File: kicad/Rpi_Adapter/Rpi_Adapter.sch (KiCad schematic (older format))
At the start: 12 parts, among them P1 Raspberry PI, SW1 SW_Push, U1 SGM811

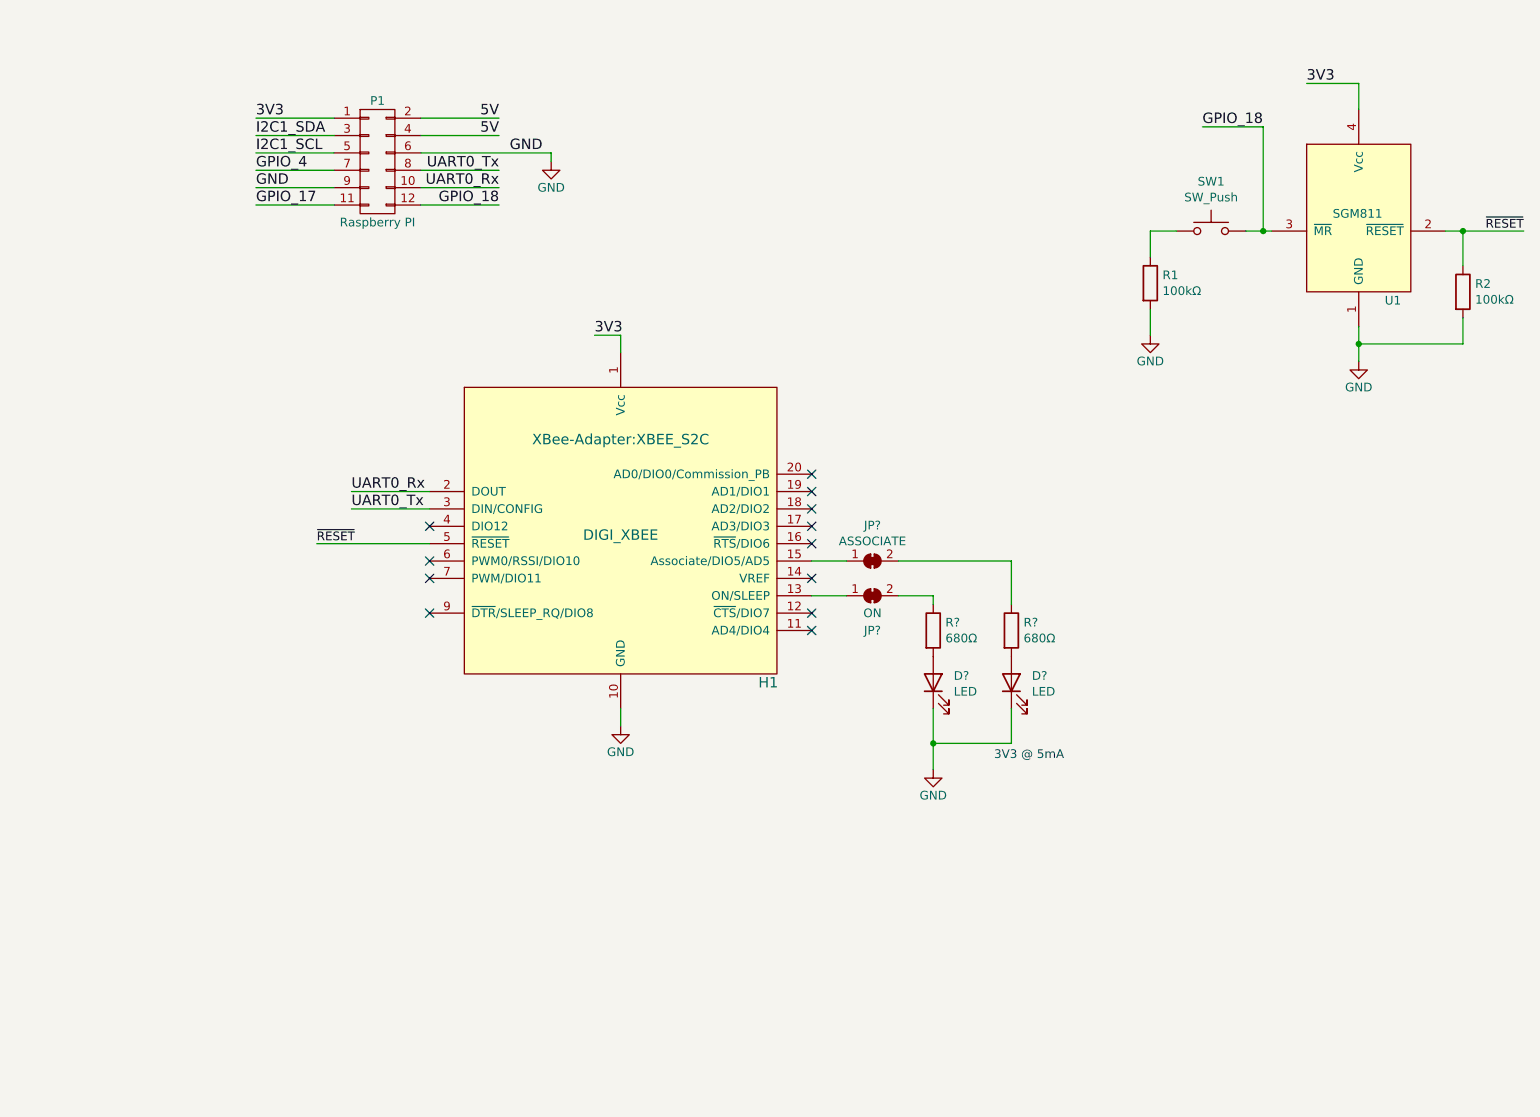
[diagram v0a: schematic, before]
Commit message: Updated the 3d view and a new layout
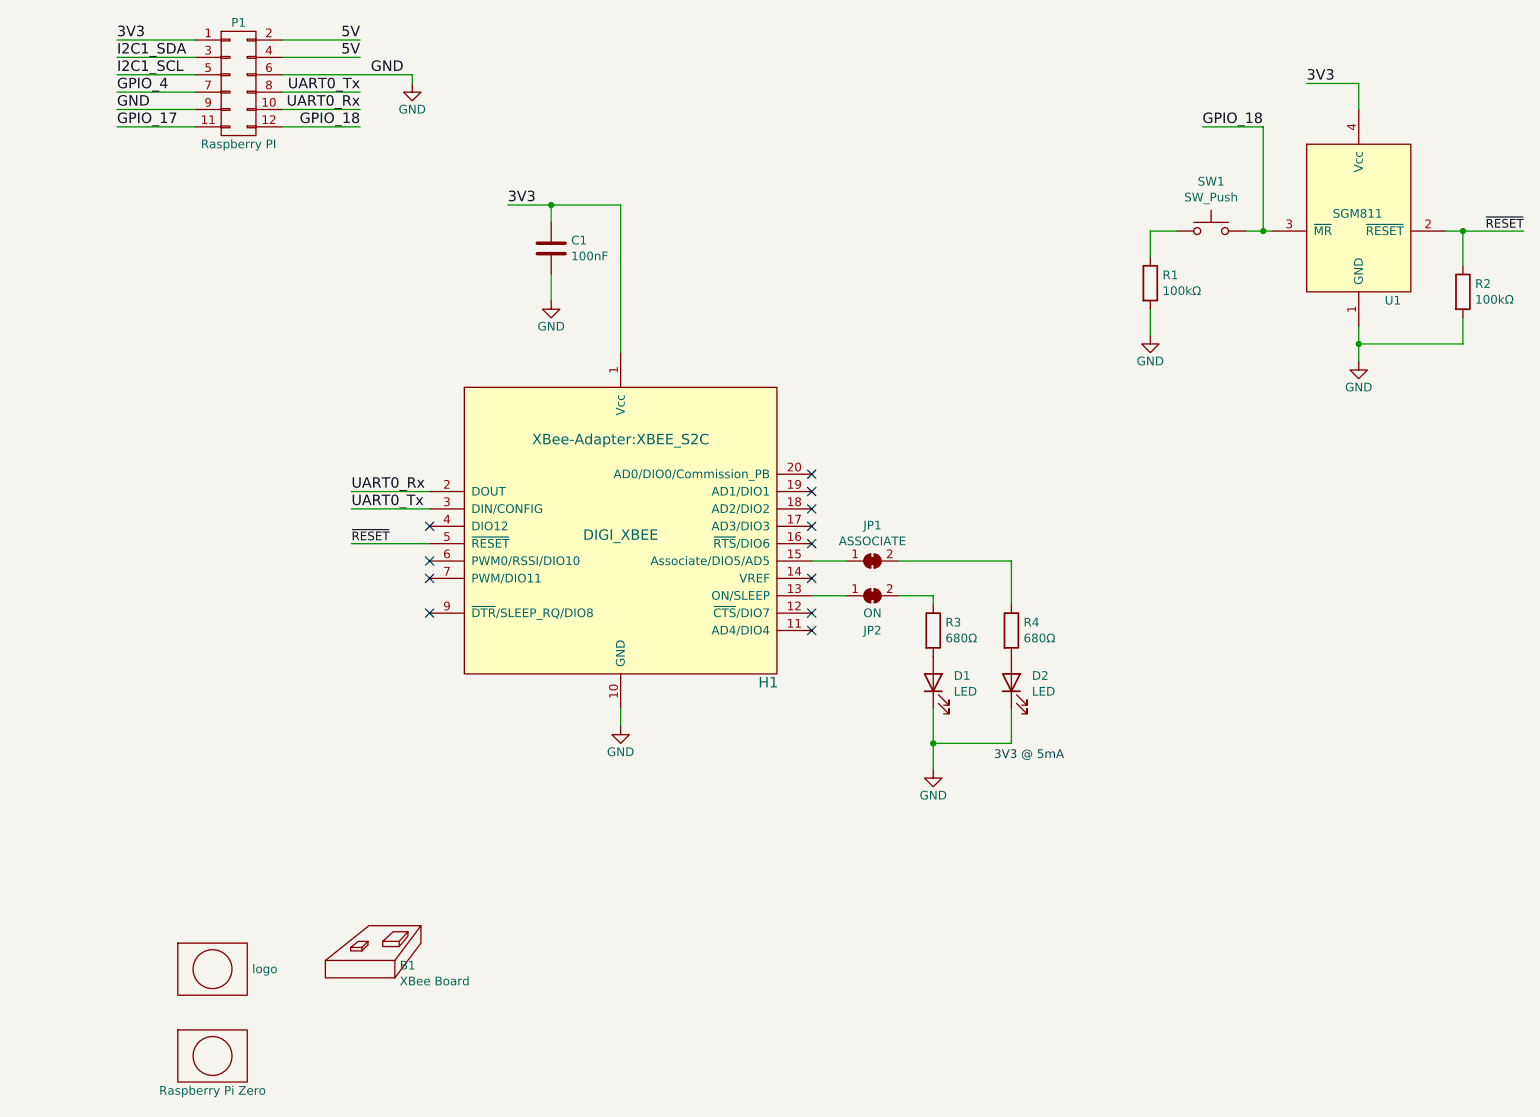
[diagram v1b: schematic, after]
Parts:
- added B1: XBee Board, mech:Board Ref, symbol mech:board
- added B2: Raspberry Pi Zero, mech:Board Ref, symbol mech:logo
- added C1: 100nF, Capacitor_SMD:C_0805_2012Metric, symbol Device:C
- added L1: logo, XBee-Adapter:MyBasic_rounded_50_1, symbol mech:logo
- D1, D2: renamed from D?; footprint (none) -> LED_SMD:LED_0805_2012Metric
- JP1, JP2: renamed from JP?; footprint (none) -> Jumper:SolderJumper-2_P1.3mm_Bridged_RoundedPad1.0x1.5mm
- R3, R4: renamed from R?; footprint (none) -> Resistor_SMD:R_0805_2012Metric
- SW1: footprint GoldCap-Check:SPST_FSM2JSMAA -> Connector_PinHeader_2.54mm:PinHeader_1x02_P2.54mm_Vertical
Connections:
- net 3V3: now also C1.1
- net GND: now also C1.2
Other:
- moved on the sheet: P1
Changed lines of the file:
@@
 Comment4 ""
 $EndDescr
-Text Label 4500 2900 0    60   ~ 0
+Text Label 4000 2150 0    60   ~ 0
 3V3
 Wire Wire Line
-	4500 2900 4650 2900
-Wire Wire Line
-	4650 2900 4650 3000
+	4000 2150 4250 2150
+Wire Wire Line
+	4650 2150 4650 3000
 $Comp
 L power:GND #PWR01
@@
 L Rpi_Adapter-rescue:CONN_02X06 P1
 U 1 1 59933EB5
-P 3250 1900
-F 0 "P1" H 3250 2250 50  0000 C CNN
-F 1 "Raspberry PI" H 3250 1550 50  0000 C CNN
-F 2 "Socket_Strips:Socket_Strip_Straight_2x06_Pitch2.54mm" H 3250 700 60  0001 C CNN
-F 3 "" H 3250 700 60  0000 C CNN
-	1    3250 1900
-	1    0    0    -1
-$EndComp
-Wire Wire Line
-	3000 1650 2550 1650
-Wire Wire Line
-	3500 1850 4250 1850
-Wire Wire Line
-	3500 1950 3950 1950
-Wire Wire Line
-	3500 2050 3950 2050
-Text Label 2550 1650 0    60   ~ 0
+P 2450 1450
+F 0 "P1" H 2450 1800 50  0000 C CNN
+F 1 "Raspberry PI" H 2450 1100 50  0000 C CNN
+F 2 "Socket_Strips:Socket_Strip_Straight_2x06_Pitch2.54mm" H 2450 250 60  0001 C CNN
+F 3 "" H 2450 250 60  0000 C CNN
+	1    2450 1450
+	1    0    0    -1
+$EndComp
+Wire Wire Line
+	2200 1200 1750 1200
+Wire Wire Line
+	2700 1400 3450 1400
+Wire Wire Line
+	2700 1500 3150 1500
+Wire Wire Line
+	2700 1600 3150 1600
+Text Label 1750 1200 0    60   ~ 0
 3V3
 $Comp
 L power:GND #PWR02
 U 1 1 5993431C
-P 4250 1900
-F 0 "#PWR02" H 4250 1650 50  0001 C CNN
-F 1 "GND" H 4250 1750 50  0000 C CNN
-F 2 "" H 4250 1900 60  0000 C CNN
-F 3 "" H 4250 1900 60  0000 C CNN
-	1    4250 1900
-	1    0    0    -1
-$EndComp
-Wire Wire Line
-	4250 1850 4250 1900
-Text Label 3950 1950 2    60   ~ 0
+P 3450 1450
+F 0 "#PWR02" H 3450 1200 50  0001 C CNN
+F 1 "GND" H 3450 1300 50  0000 C CNN
+F 2 "" H 3450 1450 60  0000 C CNN
+F 3 "" H 3450 1450 60  0000 C CNN
+	1    3450 1450
+	1    0    0    -1
+$EndComp
+Wire Wire Line
+	3450 1400 3450 1450
+Text Label 3150 1500 2    60   ~ 0
 UART0_Tx
-Text Label 3950 2050 2    60   ~ 0
+Text Label 3150 1600 2    60   ~ 0
 UART0_Rx
 Wire Wire Line
-	3500 1650 3950 1650
-Wire Wire Line
-	3500 1750 3950 1750
-Wire Wire Line
-	3000 1750 2550 1750
-Wire Wire Line
-	3000 1850 2550 1850
-Wire Wire Line
-	3000 1950 2550 1950
-Wire Wire Line
-	3000 2050 2550 2050
-Wire Wire Line
-	3000 2150 2550 2150
-Wire Wire Line
-	3500 2150 3950 2150
-Text Label 2550 1750 0    60   ~ 0
+	2700 1200 3150 1200
+Wire Wire Line
+	2700 1300 3150 1300
+Wire Wire Line
+	2200 1300 1750 1300
+Wire Wire Line
+	2200 1400 1750 1400
+Wire Wire Line
+	2200 1500 1750 1500
+Wire Wire Line
+	2200 1600 1750 1600
+Wire Wire Line
+	2200 1700 1750 1700
+Wire Wire Line
+	2700 1700 3150 1700
+Text Label 1750 1300 0    60   ~ 0
 I2C1_SDA
-Text Label 2550 1850 0    60   ~ 0
+Text Label 1750 1400 0    60   ~ 0
 I2C1_SCL
-Text Label 2550 1950 0    60   ~ 0
+Text Label 1750 1500 0    60   ~ 0
 GPIO_4
-Text Label 2550 2050 0    60   ~ 0
+Text Label 1750 1600 0    60   ~ 0
 GND
-Text Label 2550 2150 0    60   ~ 0
+Text Label 1750 1700 0    60   ~ 0
 GPIO_17
-Text Label 3950 1650 2    60   ~ 0
+Text Label 3150 1200 2    60   ~ 0
 5V
-Text Label 3950 1750 2    60   ~ 0
+Text Label 3150 1300 2    60   ~ 0
 5V
-Text Label 4200 1850 2    60   ~ 0
+Text Label 3400 1400 2    60   ~ 0
 GND
-Text Label 3950 2150 2    60   ~ 0
+Text Label 3150 1700 2    60   ~ 0
 GPIO_18
 $Comp
@@
 F 0 "SW1" H 8050 2585 50  0000 C CNN
 F 1 "SW_Push" H 8050 2494 50  0000 C CNN
-F 2 "GoldCap-Check:SPST_FSM2JSMAA" H 8050 2500 50  0001 C CNN
+F 2 "Connector_PinHeader_2.54mm:PinHeader_1x02_P2.54mm_Vertical" H 8050 2500 50  0001 C CNN
 F 3 "~" H 8050 2500 50  0001 C CNN
 	1    8050 2300
@@
 $EndComp
 Wire Wire Line
-	3550 4100 2900 4100
+	3550 4100 3100 4100
 Text Label 8000 1700 0    60   ~ 0
 GPIO_18
@@
 Wire Wire Line
 	8350 2300 8250 2300
-Text Label 2900 4100 0    50   ~ 0
+Text Label 3100 4100 0    50   ~ 0
 ~RESET
 Wire Wire Line
@@
 	5750 4400 5950 4400
 $Comp
-L Jumper:SolderJumper_2_Bridged JP?
+L Jumper:SolderJumper_2_Bridged JP1
 U 1 1 612FC7BD
 P 6100 4200
-F 0 "JP?" H 6100 4405 50  0000 C CNN
+F 0 "JP1" H 6100 4405 50  0000 C CNN
 F 1 "ASSOCIATE" H 6100 4314 50  0000 C CNN
-F 2 "" H 6100 4200 50  0001 C CNN
+F 2 "Jumper:SolderJumper-2_P1.3mm_Bridged_RoundedPad1.0x1.5mm" H 6100 4200 50  0001 C CNN
 F 3 "~" H 6100 4200 50  0001 C CNN
 	1    6100 4200
@@
 $EndComp
 $Comp
-L Jumper:SolderJumper_2_Bridged JP?
+L Jumper:SolderJumper_2_Bridged JP2
 U 1 1 612FD33D
 P 6100 4400
-F 0 "JP?" H 6100 4200 50  0000 C CNN
+F 0 "JP2" H 6100 4200 50  0000 C CNN
 F 1 "ON" H 6100 4300 50  0000 C CNN
-F 2 "" H 6100 4400 50  0001 C CNN
+F 2 "Jumper:SolderJumper-2_P1.3mm_Bridged_RoundedPad1.0x1.5mm" H 6100 4400 50  0001 C CNN
 F 3 "~" H 6100 4400 50  0001 C CNN
 	1    6100 4400
@@
 $EndComp
 $Comp
-L Device:LED D?
+L Device:LED D1
 U 1 1 612FE401
 P 6450 4900
-F 0 "D?" V 6489 4782 50  0000 R CNN
+F 0 "D1" V 6489 4782 50  0000 R CNN
 F 1 "LED" V 6398 4782 50  0000 R CNN
-F 2 "" H 6450 4900 50  0001 C CNN
+F 2 "LED_SMD:LED_0805_2012Metric" H 6450 4900 50  0001 C CNN
 F 3 "~" H 6450 4900 50  0001 C CNN
 	1    6450 4900
@@
 $EndComp
 $Comp
-L Device:LED D?
+L Device:LED D2
 U 1 1 612FF5D4
 P 6900 4900
-F 0 "D?" V 6939 4782 50  0000 R CNN
+F 0 "D2" V 6939 4782 50  0000 R CNN
 F 1 "LED" V 6848 4782 50  0000 R CNN
-F 2 "" H 6900 4900 50  0001 C CNN
+F 2 "LED_SMD:LED_0805_2012Metric" H 6900 4900 50  0001 C CNN
 F 3 "~" H 6900 4900 50  0001 C CNN
 	1    6900 4900
@@
 	6450 5250 6450 5400
 $Comp
-L power:GND #PWR?
+L power:GND #PWR0101
 U 1 1 61300F5E
 P 6450 5400
-F 0 "#PWR?" H 6450 5150 50  0001 C CNN
+F 0 "#PWR0101" H 6450 5150 50  0001 C CNN
 F 1 "GND" H 6450 5250 50  0000 C CNN
 F 2 "" H 6450 5400 60  0000 C CNN
@@
 $EndComp
 $Comp
-L Device:R R?
+L Device:R R3
 U 1 1 61301AD8
 P 6450 4600
-F 0 "R?" H 6520 4646 50  0000 L CNN
+F 0 "R3" H 6520 4646 50  0000 L CNN
 F 1 "680Ω" H 6520 4555 50  0000 L CNN
-F 2 "" V 6380 4600 50  0001 C CNN
+F 2 "Resistor_SMD:R_0805_2012Metric" V 6380 4600 50  0001 C CNN
 F 3 "~" H 6450 4600 50  0001 C CNN
 	1    6450 4600
@@
 $EndComp
 $Comp
-L Device:R R?
+L Device:R R4
 U 1 1 61301FA2
 P 6900 4600
-F 0 "R?" H 6970 4646 50  0000 L CNN
+F 0 "R4" H 6970 4646 50  0000 L CNN
 F 1 "680Ω" H 6970 4555 50  0000 L CNN
-F 2 "" V 6830 4600 50  0001 C CNN
+F 2 "Resistor_SMD:R_0805_2012Metric" V 6830 4600 50  0001 C CNN
 F 3 "~" H 6900 4600 50  0001 C CNN
 	1    6900 4600
@@
 Text Notes 6800 5350 0    50   ~ 0
 3V3 @ 5mA
+$Comp
+L Device:C C1
+U 1 1 612E681C
+P 4250 2400
+F 0 "C1" H 4365 2446 50  0000 L CNN
+F 1 "100nF" H 4365 2355 50  0000 L CNN
+F 2 "Capacitor_SMD:C_0805_2012Metric" H 4288 2250 50  0001 C CNN
+F 3 "~" H 4250 2400 50  0001 C CNN
+	1    4250 2400
+	1    0    0    -1
+$EndComp
+Wire Wire Line
+	4250 2150 4250 2250
+Wire Wire Line
+	4250 2550 4250 2700
+Connection ~ 4250 2150
+Wire Wire Line
+	4250 2150 4650 2150
+$Comp
+L power:GND #PWR05
+U 1 1 612E794A
+P 4250 2700
+F 0 "#PWR05" H 4250 2450 50  0001 C CNN
+F 1 "GND" H 4250 2550 50  0000 C CNN
+F 2 "" H 4250 2700 60  0000 C CNN
+F 3 "" H 4250 2700 60  0000 C CNN
+	1    4250 2700
+	1    0    0    -1
+$EndComp
+$Comp
+L mech:logo L1
+U 1 1 612E7975
+P 2300 6550
+F 0 "L1" H 2300 6550 50  0001 C CNN
+F 1 "logo" H 2528 6550 50  0000 L CNN
+F 2 "XBee-Adapter:MyBasic_rounded_50_1" H 2300 6550 50  0001 C CNN
+F 3 "" H 2300 6550 50  0001 C CNN
+	1    2300 6550
+	1    0    0    -1
+$EndComp
+$Comp
+L mech:board B1
+U 1 1 612EB311
+P 3150 6550
+F 0 "B1" H 3378 6571 50  0000 L CNN
+F 1 "XBee Board" H 3378 6480 50  0000 L CNN
+F 2 "mech:Board Ref" H 3150 6550 50  0001 C CNN
+F 3 "" H 3150 6550 50  0001 C CNN
+	1    3150 6550
+	1    0    0    -1
+$EndComp
+$Comp
+L mech:logo B2
+U 1 1 612ECCDF
+P 2300 7050
+F 0 "B2" H 2300 7050 50  0001 C CNN
+F 1 "Raspberry Pi Zero" H 2300 6850 50  0000 C CNN
+F 2 "mech:Board Ref" H 2300 7050 50  0001 C CNN
+F 3 "" H 2300 7050 50  0001 C CNN
+	1    2300 7050
+	1    0    0    -1
+$EndComp
 $EndSCHEMATC

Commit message: Completed the layout and routing, Sent to OSH Park
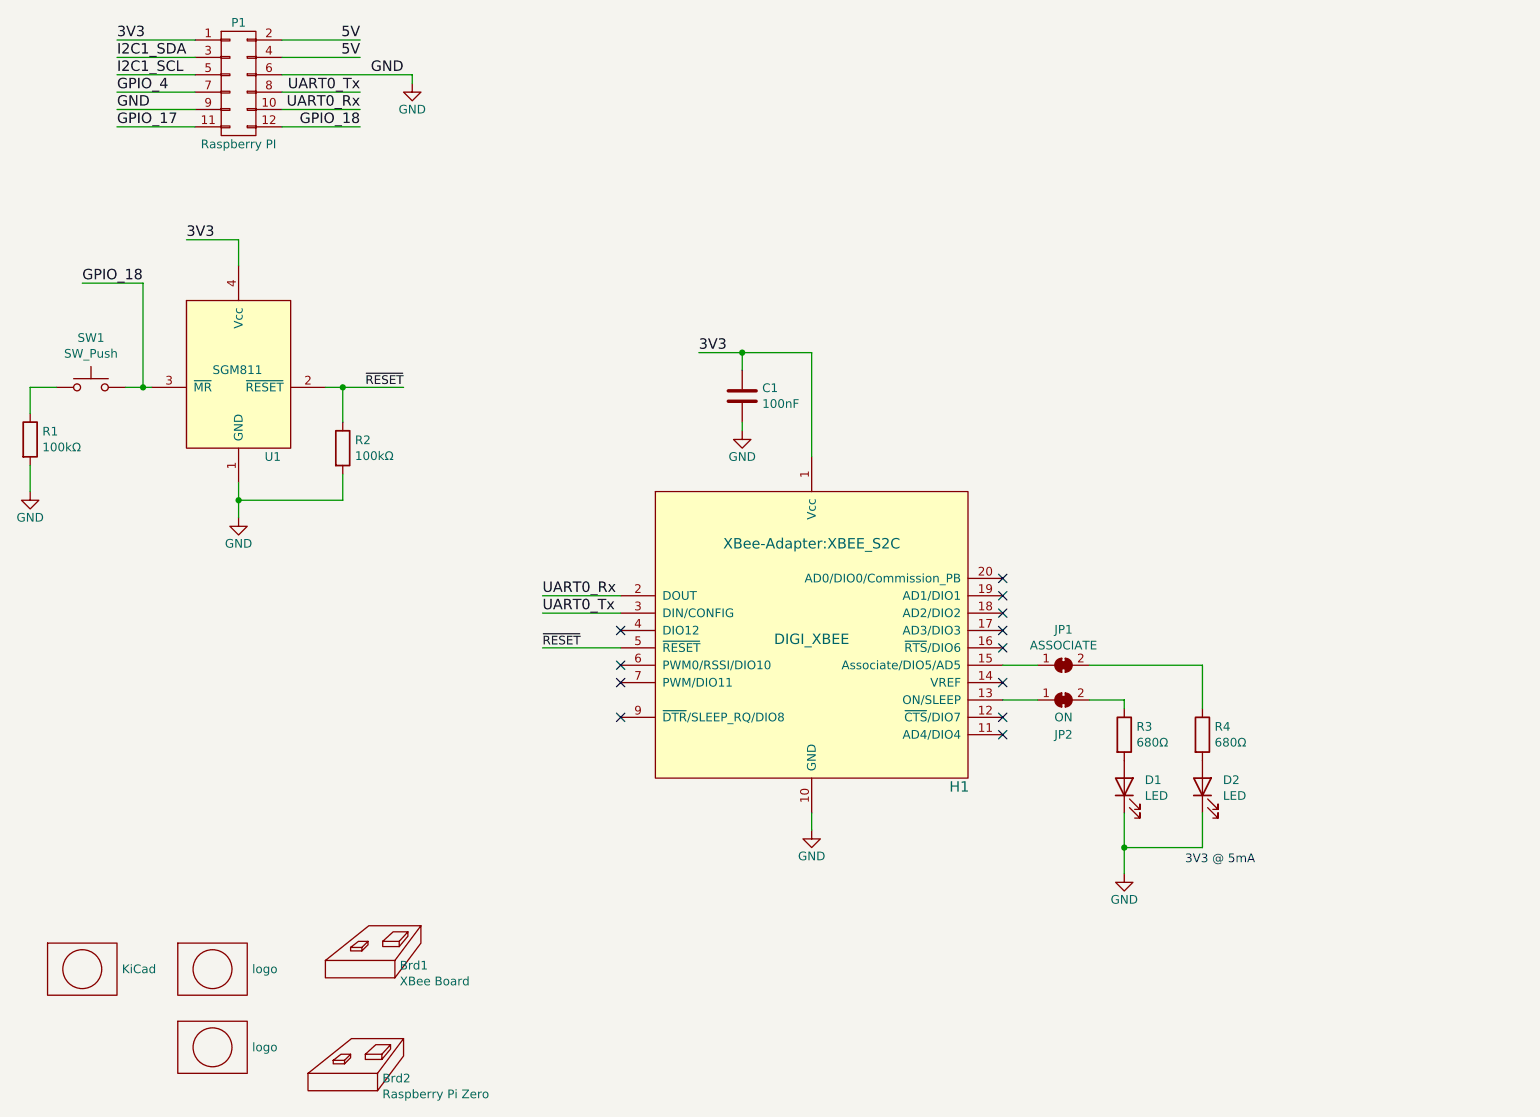
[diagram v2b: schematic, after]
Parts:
- removed B2: Raspberry Pi Zero, mech:Board Ref, symbol mech:logo
- added Brd2: Raspberry Pi Zero, mech:Board Ref, symbol mech:board
- added Lg2: KiCad, Symbols:KiCad-Logo2_6mm_SilkScreen, symbol mech:logo
- added Lg3: logo, XBee-Adapter:MyBasic_rounded_50_1, symbol mech:logo
- renumbered B1 to Brd1, L1 to Lg1
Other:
- moved on the sheet: C1, D1, D2, H1, JP1, JP2, R1, R2, R3, R4, SW1, U1
